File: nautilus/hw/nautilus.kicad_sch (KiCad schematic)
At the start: 120 parts, among them IC1 DRV8353SRTAR, IC2 STM32G474CEU6, IC3 MAX15062AATA+T, J1 XT30XT30PW_MALE, J2 Conn_01x02_Pin, J3 Conn_01x02_Pin, J4 Conn_01x02_Pin, M1 PAD24AWG_PAD, M2 PAD24AWG_PAD, M3 PAD24AWG_PAD, SW1 SW_Push, U2 CSD88599Q5DCT, U3 CSD88599Q5DCT, U4 AS5147, U5 CSD88599Q5DCT, U7 SN65HVD232

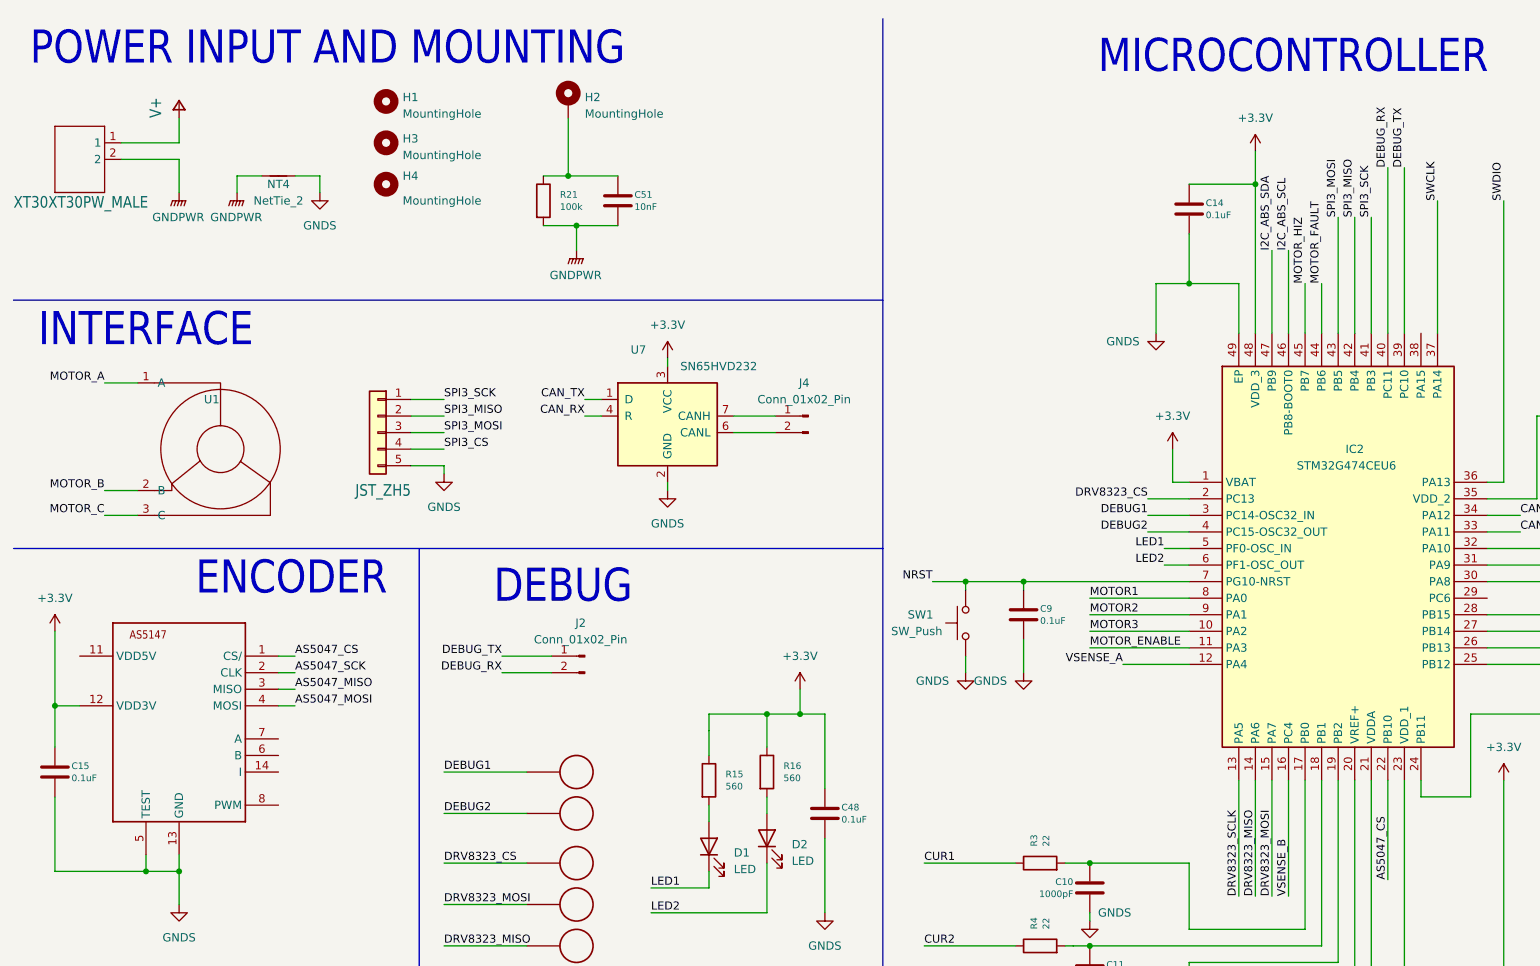
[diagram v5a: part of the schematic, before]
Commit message: First prototype assembly
 - [hw] Fix reverse XT-30 connector in PCB
 - [sw] Add led blink to SPI communication
 - [sw] Add note about using SPI1 mode only (other modes don't work)
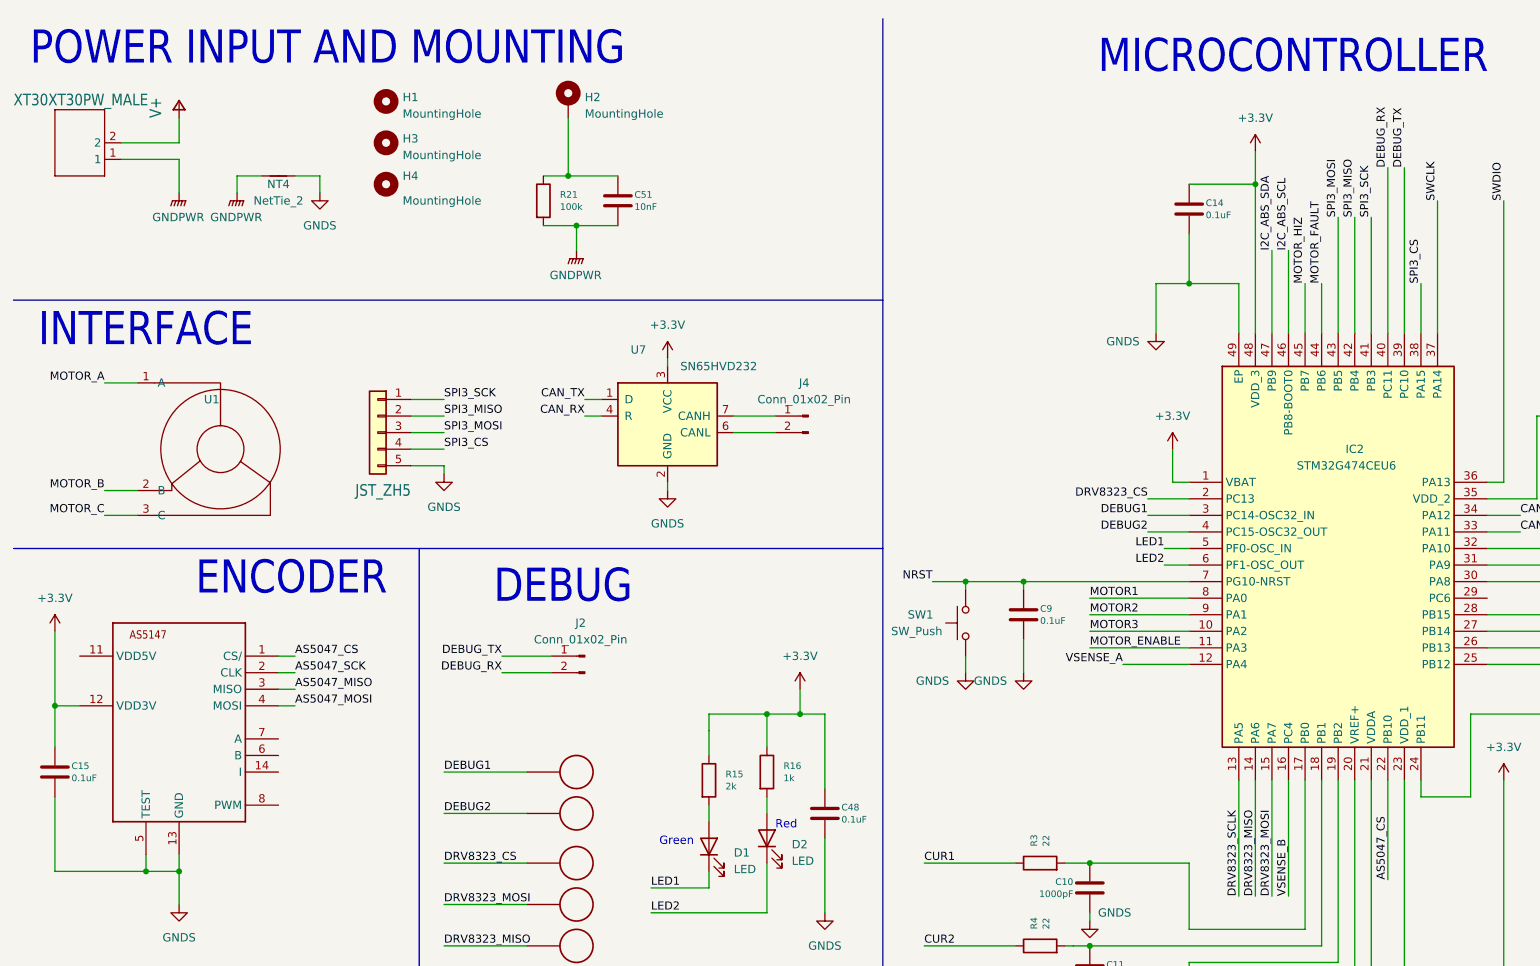
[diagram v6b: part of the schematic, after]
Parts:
- R15: value 560 -> 2k
- R16: value 560 -> 1k
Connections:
- net GNDPWR: now also J1.1; no longer J1.2
- net SPI3_CS: now also IC2.38 (PA15)
- net V+: now also J1.2; no longer J1.1
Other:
- note added: "Green"
- note added: "Red"
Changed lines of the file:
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@@
     (stroke (width 0) (type default))
   )
+  (wire (pts (xy 228.6 53.34) (xy 228.6 60.96))
+    (stroke (width 0) (type default))
+  )
   (wire (pts (xy 218.44 326.39) (xy 218.44 327.66))
     (stroke (width 0) (type default))
@@
     (stroke (width 0.1524) (type solid))
   )
-  (wire (pts (xy 29.21 34.29) (xy 38.1 34.29))
-    (stroke (width 0.1524) (type solid))
-  )
   (wire (pts (xy 243.84 224.79) (xy 243.84 226.06))
     (stroke (width 0) (type default))
@@
     (stroke (width 0) (type default))
   )
+  (wire (pts (xy 29.21 34.29) (xy 38.1 34.29))
+    (stroke (width 0.1524) (type solid))
+  )
   (wire (pts (xy 128.27 149.86) (xy 110.49 149.86))
     (stroke (width 0.1524) (type solid))
@@
     (stroke (width 0) (type default))
   )
+  (text "Green" (at 111.76 139.7 0)
+    (effects (font (size 1.27 1.27)) (justify left bottom))
+  )
   (text "INTERFACE" (at 16.51 63.5 0)
     (effects (font (size 5.08 4.318)) (justify left bottom))
@@
     (effects (font (size 5.08 4.318)) (justify left bottom))
   )
+  (text "Red" (at 129.54 137.16 0)
+    (effects (font (size 1.27 1.27)) (justify left bottom))
+  )
   (text "MICROCONTROLLER" (at 179.07 21.59 0)
     (effects (font (size 5.08 4.318)) (justify left bottom))
@@
     (effects (font (size 1.2446 1.2446)) (justify left bottom))
   )
+  (label "SPI3_CS" (at 228.6 53.34 90) (fields_autoplaced)
+    (effects (font (size 1.2446 1.2446)) (justify left bottom))
+  )
   (label "SPI3_MOSI" (at 78.74 76.2 0) (fields_autoplaced)
     (effects (font (size 1.2446 1.2446)) (justify left bottom))
@@
       (effects (font (size 1.016 1.016)) (justify left top))
     )
-    (property "Value" "560" (at 130.81 129.794 0)
+    (property "Value" "1k" (at 130.81 129.794 0)
       (effects (font (size 1.016 1.016)) (justify left bottom))
     )
@@
       (effects (font (size 1.016 1.016)) (justify left top))
     )
-    (property "Value" "560" (at 121.92 131.064 0)
+    (property "Value" "2k" (at 121.92 131.064 0)
       (effects (font (size 1.016 1.016)) (justify left bottom))
     )
@@
     )
   )
-  (symbol (lib_id "nautilus-eagle-import:XT30XT30PW_MALE") (at 24.13 34.29 0) (unit 1)
+  (symbol (lib_id "nautilus-eagle-import:XT30XT30PW_MALE") (at 24.13 31.75 0) (mirror x) (unit 1)
     (in_bom yes) (on_board yes) (dnp no)
-    (property "Reference" "J1" (at 19.05 28.448 0)
+    (property "Reference" "J1" (at 19.05 37.592 0)
       (effects (font (size 1.778 1.5113)) (justify left bottom) hide)
     )
-    (property "Value" "XT30XT30PW_MALE" (at 12.7 41.91 0)
+    (property "Value" "XT30XT30PW_MALE" (at 12.7 24.13 0)
       (effects (font (size 1.778 1.5113)) (justify left bottom))
     )
-    (property "Footprint" "Connector_AMASS:AMASS_XT30PW-M_1x02_P2.50mm_Horizontal" (at 24.13 34.29 0)
+    (property "Footprint" "Connector_AMASS:AMASS_XT30PW-M_1x02_P2.50mm_Horizontal" (at 24.13 31.75 0)
       (effects (font (size 1.27 1.27)) hide)
     )
-    (property "Datasheet" "" (at 24.13 34.29 0)
+    (property "Datasheet" "" (at 24.13 31.75 0)
       (effects (font (size 1.27 1.27)) hide)
     )
-    (property "POPULATE" "1" (at 24.13 34.29 0)
+    (property "POPULATE" "1" (at 24.13 31.75 0)
       (effects (font (size 1.27 1.27)) (justify left bottom) hide)
     )
-    (property "RS" "    180-5359" (at 24.13 34.29 0)
+    (property "RS" "    180-5359" (at 24.13 31.75 0)
       (effects (font (size 1.27 1.27)) hide)
     )

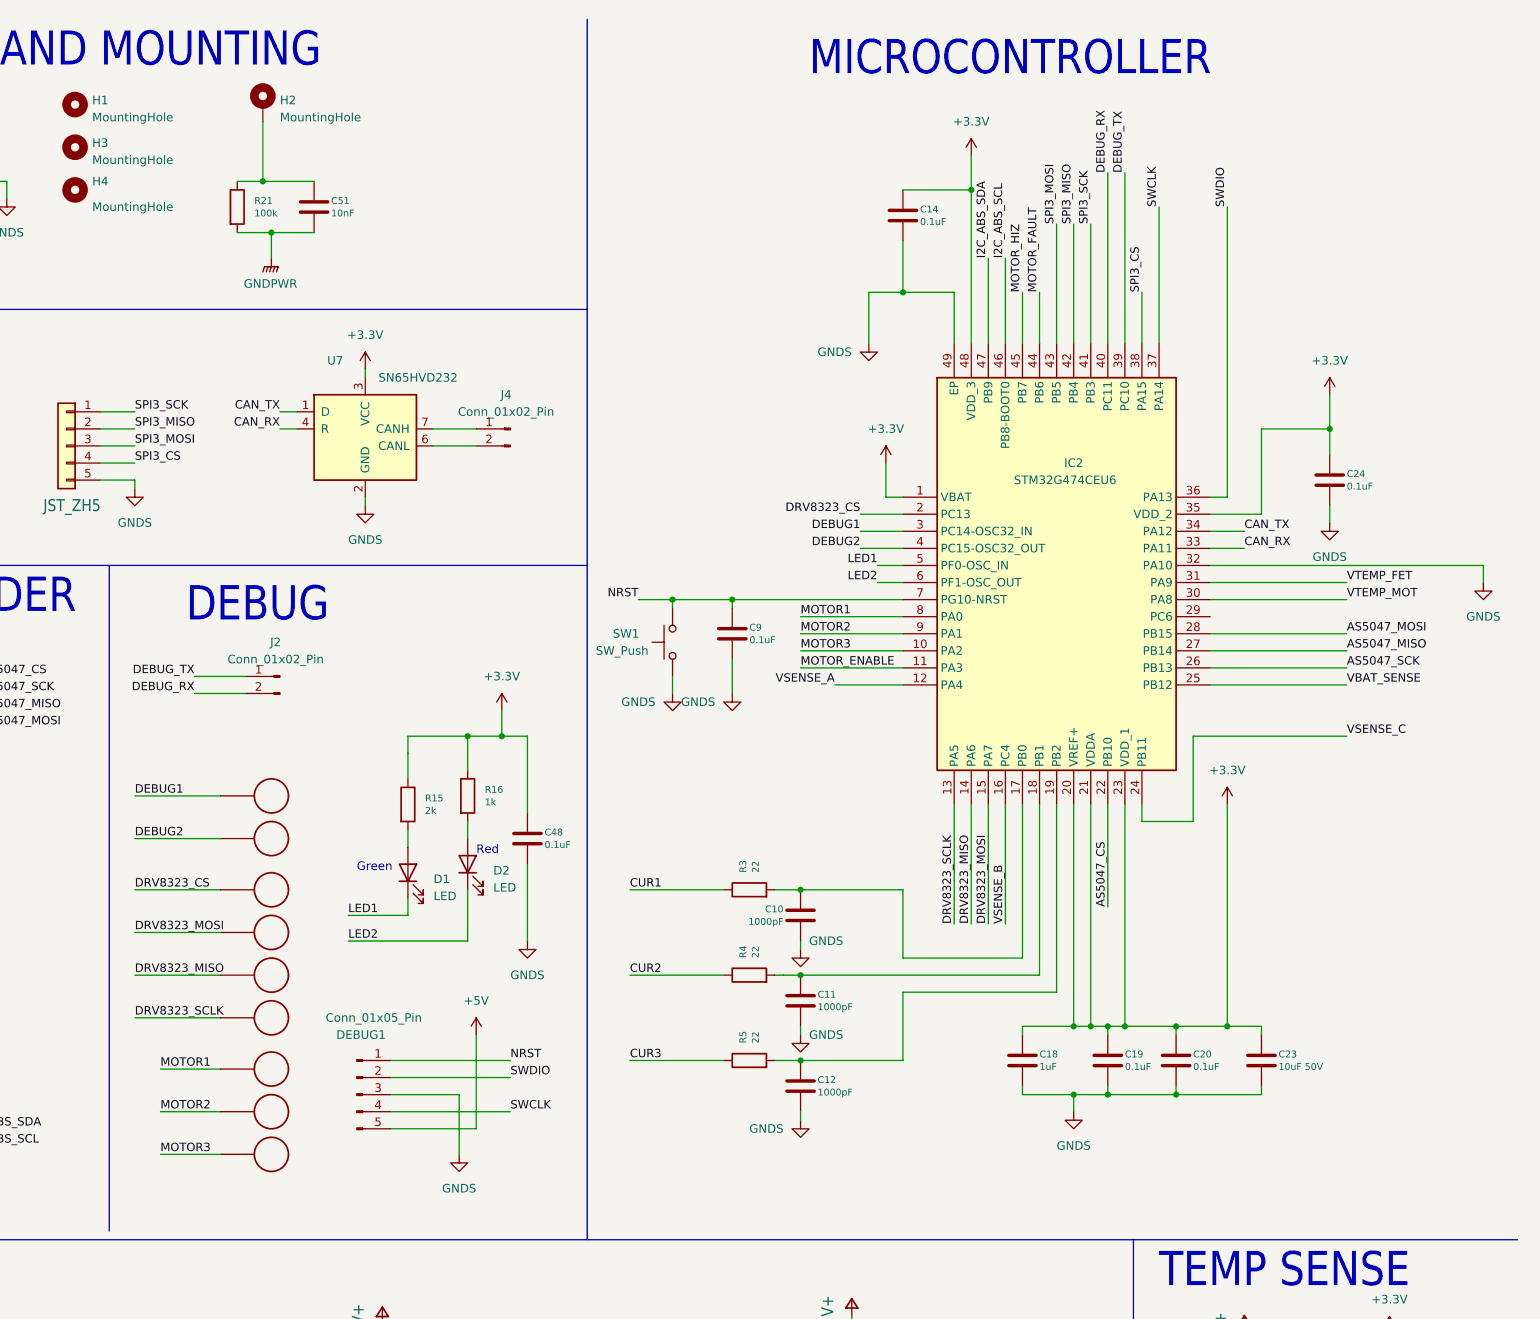
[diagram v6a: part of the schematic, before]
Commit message: [Hardware] PCB V2: new layout, using LQFP package for microcontroller.
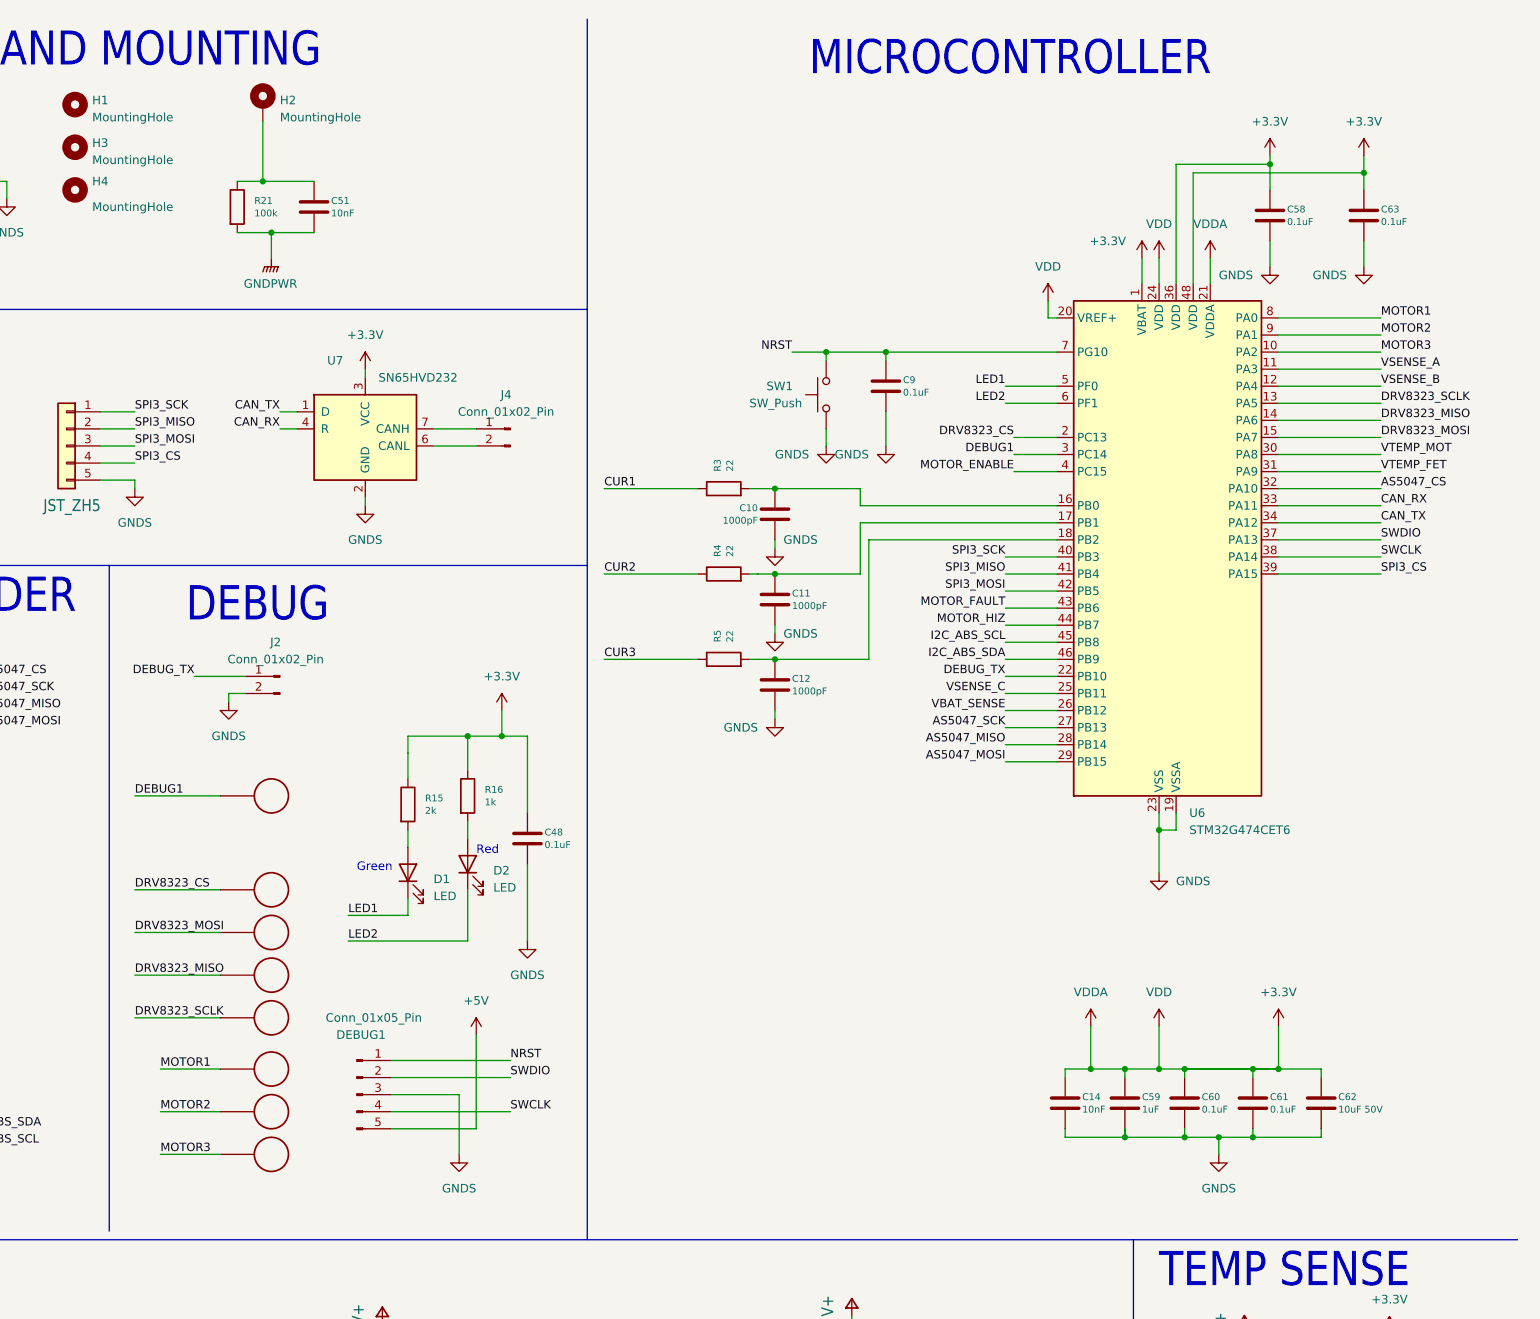
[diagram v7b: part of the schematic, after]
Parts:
- removed C18: 1uF, Capacitor_SMD:C_0402_1005Metric_Pad0.74x0.62mm_HandSolder, symbol Device:C
- removed C19, C20, C24: 0.1uF, Capacitor_SMD:C_0402_1005Metric_Pad0.74x0.62mm_HandSolder, symbol Device:C
- removed C23: 10uF 50V, Capacitor_SMD:C_1206_3216Metric_Pad1.33x1.80mm_HandSolder, symbol Device:C
- removed DBG2: PAD24AWG_PAD, TestPoint:TestPoint_Pad_D1.0mm, symbol nautilus-eagle-import:PAD24AWG_PAD
- removed IC2: STM32G474CEU6, nautilus:QFN50P700X700X60-49N-D, symbol nautilus:STM32G474CEU6
- added C58, C60, C61, C63: 0.1uF, Capacitor_SMD:C_0402_1005Metric_Pad0.74x0.62mm_HandSolder, symbol Device:C
- added C59: 1uF, Capacitor_SMD:C_0402_1005Metric_Pad0.74x0.62mm_HandSolder, symbol Device:C
- added C62: 10uF 50V, Capacitor_SMD:C_1206_3216Metric_Pad1.33x1.80mm_HandSolder, symbol Device:C
- added U6: STM32G474CET6, Package_QFP:LQFP-48_7x7mm_P0.5mm, symbol MCU_ST_STM32G4:STM32G474CETx
- C14: value 0.1uF -> 10nF; HOUSEPART YES -> 1; MPN MF-CAP-0402-0.1uF -> MF-CAP-0402-1nF; POPULATE (none) -> 1; RS 247-7824 -> 242-7313
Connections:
- net DEBUG_RX is gone; now on net GNDS: J2.2 (Pin_2)
- net +3.3V: now also C58.1, C59.1, C60.1, C61.1, C62.1, C63.1, U6.1 (VBAT), U6.20 (VREF+), U6.21 (VDDA), U6.24 (VDD), U6.36 (VDD), U6.48 (VDD)
- net AS5047_CS: now also U6.32 (PA10)
- net AS5047_MISO: now also U6.28 (PB14)
- net AS5047_MOSI: now also U6.29 (PB15)
- net AS5047_SCK: now also U6.27 (PB13)
- net CAN_RX: now also U6.33 (PA11)
- net CAN_TX: now also U6.34 (PA12)
- net DEBUG1: now also U6.3 (PC14)
- net DEBUG_TX: now also U6.22 (PB10)
- net DRV8323_CS: now also U6.2 (PC13)
- net DRV8323_MISO: now also U6.14 (PA6)
- net DRV8323_MOSI: now also U6.15 (PA7)
- net DRV8323_SCLK: now also U6.13 (PA5)
- net GNDS: now also C58.2, C59.2, C60.2, C61.2, C62.2, C63.2, U6.19 (VSSA), U6.23 (VSS), U6.35 (VSS), U6.47 (VSS)
- net I2C_ABS_SCL: now also U6.45 (PB8)
- net I2C_ABS_SDA: now also U6.46 (PB9)
- net LED1: now also U6.5 (PF0)
- net LED2: now also U6.6 (PF1)
- net MOTOR1: now also U6.8 (PA0)
- net MOTOR2: now also U6.9 (PA1)
- net MOTOR3: now also U6.10 (PA2)
- net MOTOR_ENABLE: now also U6.4 (PC15)
- net MOTOR_FAULT: now also U6.43 (PB6)
- net MOTOR_HIZ: now also U6.44 (PB7)
- net NRST: now also U6.7 (PG10)
- net SPI3_CS: now also U6.39 (PA15)
- net SPI3_MISO: now also U6.41 (PB4)
- net SPI3_MOSI: now also U6.42 (PB5)
- net SPI3_SCK: now also U6.40 (PB3)
- net SWCLK: now also U6.38 (PA14)
- net SWDIO: now also U6.37 (PA13)
- net VBAT_SENSE: now also U6.26 (PB12)
- net VSENSE_A: now also U6.11 (PA3)
- net VSENSE_B: now also U6.12 (PA4)
- net VSENSE_C: now also U6.25 (PB11)
- net VTEMP_FET: now also U6.31 (PA9)
- net VTEMP_MOT: now also U6.30 (PA8)
- net at C11.1, R4.2: now also U6.17 (PB1)
- net at C12.1, R5.2: now also U6.18 (PB2)
- net at C10.1, R3.2: now also U6.16 (PB0)

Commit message: [Hardware] V2 board order
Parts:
- C28, C29, C31, C32, C34, C35, C36, C37, C38, C39, C40, C41, C42, C43, C44, C45, C47, C53, C54, C55, C56, C57, C62: MPN C3216X7R1H106K160AE -> CL31A106MBHNNNE; Mouser Part Number (none) -> 187-CL31A106MBHNNNE; RS 165-6471 -> (none)
- U6: Mouser 511-STM32G474CET6 -> (none); Mouser Part Number (none) -> 511-STM32G474CET6
